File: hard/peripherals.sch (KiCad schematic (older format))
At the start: 16 parts, among them J3 PJ-3062-CO, U1 DNP, U2 ADXL345BCCZ-RL7

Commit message: attribute naming update
JLCPCB_Part_Number -> LCSC
DigiKey_Part_Number -> DigiKey
Mouser_Part_Number -> Mouser
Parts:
- D1026, D1027: JLCPCB_Part_Number C8056 -> (none); LCSC (none) -> C8056
- D1028: JLCPCB_Part_Number C32677 -> (none); LCSC (none) -> C32677
- D?: DigiKey (none) -> LTST-S270TBKT-5A-ND; DigiKey_Part_Number LTST-S270TBKT-5A-ND -> (none); JLCPCB_Part_Number C125115 -> (none); LCSC (none) -> C125115; Mouser (none) -> 859-LTST-S270TBKT; Mouser_Part_Number 859-LTST-S270TBKT -> (none)
- J3: JLCPCB_Part_Number C319113 -> (none); LCSC (none) -> C319113
- M?: JLCPCB_Part_Number C65189 -> (none); LCSC (none) -> C65189
- U1: DigiKey (none) -> ADXL362BCCZ-RL7CT-ND; DigiKey_Part_Number ADXL362BCCZ-RL7CT-ND -> (none); JLCPCB_Part_Number C59641 -> (none); LCSC (none) -> C59641
- U2: DigiKey (none) -> ADXL345BCCZ-RLCT-ND; DigiKey_Part_Number ADXL345BCCZ-RLCT-ND -> (none); JLCPCB_Part_Number C9667 -> (none); LCSC (none) -> C9667
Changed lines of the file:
@@
 F 2 "led_matrix:Sensors_AnalogDevices_ADXL345BCCZ-RL" H 8750 4300 50  0001 C CNN
 F 3 "https://www.analog.com/media/en/technical-documentation/data-sheets/ADXL345.pdf" H 8750 4800 50  0001 C CNN
-F 4 "ADXL345BCCZ-RLCT-ND" H 8750 4300 50  0001 C CNN "DigiKey_Part_Number"
-F 5 "C9667" H 8750 4300 50  0001 C CNN "JLCPCB_Part_Number"
+F 4 "ADXL345BCCZ-RLCT-ND" H 8750 4300 50  0001 C CNN "DigiKey"
+F 5 "C9667" H 8750 4300 50  0001 C CNN "LCSC"
 F 6 "Analog Devices Inc." H 8750 4300 50  0001 C CNN "MF"
 F 7 "ADXL345BCCZ-RL7" H 8750 4300 50  0001 C CNN "MPN"
@@
 F 2 "led_matrix:Connectors_XKB Connectivity_PJ-3062-CO" H 2400 2650 50  0001 C CNN
 F 3 "2002271743_XKB-Connectivity-PJ-3062-CO_C319113.pdf" H 2400 2650 50  0001 C CNN
-F 4 "" H 2400 2650 50  0001 C CNN "DigiKey_Part_Number"
-F 5 "" H 2400 2650 50  0001 C CNN "Mouser_Part_Number"
-F 6 "C319113" H 2400 2650 50  0001 C CNN "JLCPCB_Part_Number"
+F 4 "" H 2400 2650 50  0001 C CNN "DigiKey"
+F 5 "" H 2400 2650 50  0001 C CNN "Mouser"
+F 6 "C319113" H 2400 2650 50  0001 C CNN "LCSC"
 F 7 "XKB Connectivity" H 2400 2650 50  0001 C CNN "MF"
 F 8 "PJ-3062-CO" H 2400 2650 50  0001 C CNN "MPN"
@@
 F 2 "Package_TO_SOT_SMD:SOT-23" H 3250 3200 50  0001 C CNN
 F 3 "ProTek-Devices-PSM712-LF-T7_C32677.pdf" H 3250 3200 50  0001 C CNN
-F 4 "" H 3250 3200 50  0001 C CNN "DigiKey_Part_Number"
-F 5 "" H 3250 3200 50  0001 C CNN "Mouser_Part_Number"
-F 6 "C32677" H 3250 3200 50  0001 C CNN "JLCPCB_Part_Number"
+F 4 "" H 3250 3200 50  0001 C CNN "DigiKey"
+F 5 "" H 3250 3200 50  0001 C CNN "Mouser"
+F 6 "C32677" H 3250 3200 50  0001 C CNN "LCSC"
 F 7 "ProTek Devices" H 3250 3200 50  0001 C CNN "MF"
 F 8 "PSM712-LF-T7" H 3250 3200 50  0001 C CNN "MPN"
@@
 F 2 "Diode_SMD:D_MiniMELF" H 3750 3150 50  0001 C CNN
 F 3 "1812121407_Semtech-ZMM3V3_C8056.pdf" H 3750 3150 50  0001 C CNN
-F 4 "" V 3750 3150 50  0001 C CNN "DigiKey_Part_Number"
-F 5 "" V 3750 3150 50  0001 C CNN "Mouser_Part_Number"
-F 6 "C8056" V 3750 3150 50  0001 C CNN "JLCPCB_Part_Number"
+F 4 "" V 3750 3150 50  0001 C CNN "DigiKey"
+F 5 "" V 3750 3150 50  0001 C CNN "Mouser"
+F 6 "C8056" V 3750 3150 50  0001 C CNN "LCSC"
 F 7 "ZMM3V3" V 3750 3150 50  0001 C CNN "MF"
 F 8 "Semtech" V 3750 3150 50  0001 C CNN "MPN"
@@
 F 2 "Diode_SMD:D_MiniMELF" H 4250 3150 50  0001 C CNN
 F 3 "1812121407_Semtech-ZMM3V3_C8056.pdf" H 4250 3150 50  0001 C CNN
-F 4 "" V 4250 3150 50  0001 C CNN "DigiKey_Part_Number"
-F 5 "" V 4250 3150 50  0001 C CNN "Mouser_Part_Number"
-F 6 "C8056" V 4250 3150 50  0001 C CNN "JLCPCB_Part_Number"
+F 4 "" V 4250 3150 50  0001 C CNN "DigiKey"
+F 5 "" V 4250 3150 50  0001 C CNN "Mouser"
+F 6 "C8056" V 4250 3150 50  0001 C CNN "LCSC"
 F 7 "ZMM3V3" V 4250 3150 50  0001 C CNN "MF"
 F 8 "Semtech" V 4250 3150 50  0001 C CNN "MPN"
@@
 F 2 "led_matrix:Sensors_AnalogDevices_ADXL362BCCZ-RX" H 8600 2750 50  0001 C CNN
 F 3 "https://www.analog.com/media/en/technical-documentation/data-sheets/ADXL362.pdf" H 8600 3250 50  0001 C CNN
-F 4 "ADXL362BCCZ-RL7CT-ND" H 8500 2750 50  0001 C CNN "DigiKey_Part_Number"
-F 5 "C59641" H 8600 2750 50  0001 C CNN "JLCPCB_Part_Number"
+F 4 "ADXL362BCCZ-RL7CT-ND" H 8500 2750 50  0001 C CNN "DigiKey"
+F 5 "C59641" H 8600 2750 50  0001 C CNN "LCSC"
 F 6 "Analog Devices" H 8500 2750 50  0001 C CNN "MF"
 F 7 "ADXL362BCCZ-RL" H 8500 2750 50  0001 C CNN "MPN"
@@
 F 2 "led_matrix:LED_LiteOn_LTST-S270TBKT" H 3850 5400 50  0001 C CNN
 F 3 "https://datasheet.lcsc.com/szlcsc/1810231514_Lite-On-LTST-S270TBKT_C125115.pdf" H 3850 5400 50  0001 C CNN
-F 4 "LTST-S270TBKT-5A-ND" H 3800 5300 50  0001 C CNN "DigiKey_Part_Number"
-F 5 "859-LTST-S270TBKT" H 3800 5300 50  0001 C CNN "Mouser_Part_Number"
-F 6 "C125115" H 3800 5300 50  0001 C CNN "JLCPCB_Part_Number"
+F 4 "LTST-S270TBKT-5A-ND" H 3800 5300 50  0001 C CNN "DigiKey"
+F 5 "859-LTST-S270TBKT" H 3800 5300 50  0001 C CNN "Mouser"
+F 6 "C125115" H 3800 5300 50  0001 C CNN "LCSC"
 F 7 "Lite-On Inc." H 3800 5300 50  0001 C CNN "MF"
 F 8 "LTST-S270TBKT" H 3800 5300 50  0001 C CNN "MPN"
@@
 F 2 "Package_TO_SOT_SMD:SOT-23" H 4550 5950 50  0001 C CNN
 F 3 "https://assets.nexperia.com/documents/data-sheet/2N7002.pdf" H 3750 5950 50  0001 C CNN
-F 4 "C65189" H 4150 5850 50  0001 C CNN "JLCPCB_Part_Number"
+F 4 "C65189" H 4150 5850 50  0001 C CNN "LCSC"
 F 5 "Nexperia" H 4550 5950 50  0001 C CNN "MF"
 F 6 "2N7002,215" H 4550 5950 50  0001 C CNN "MPN"

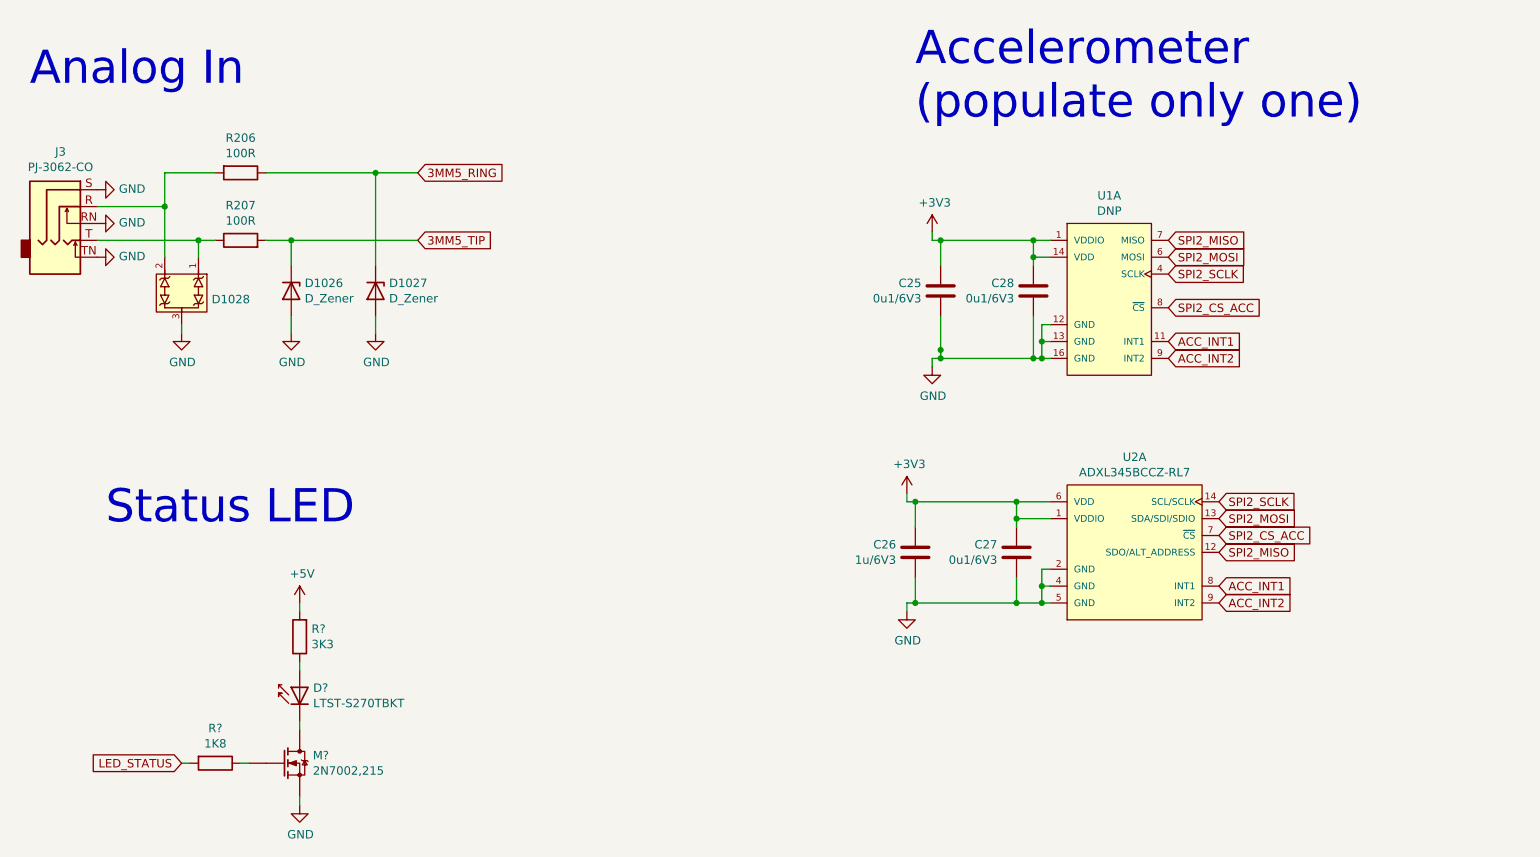
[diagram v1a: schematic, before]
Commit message: re-connect footprints
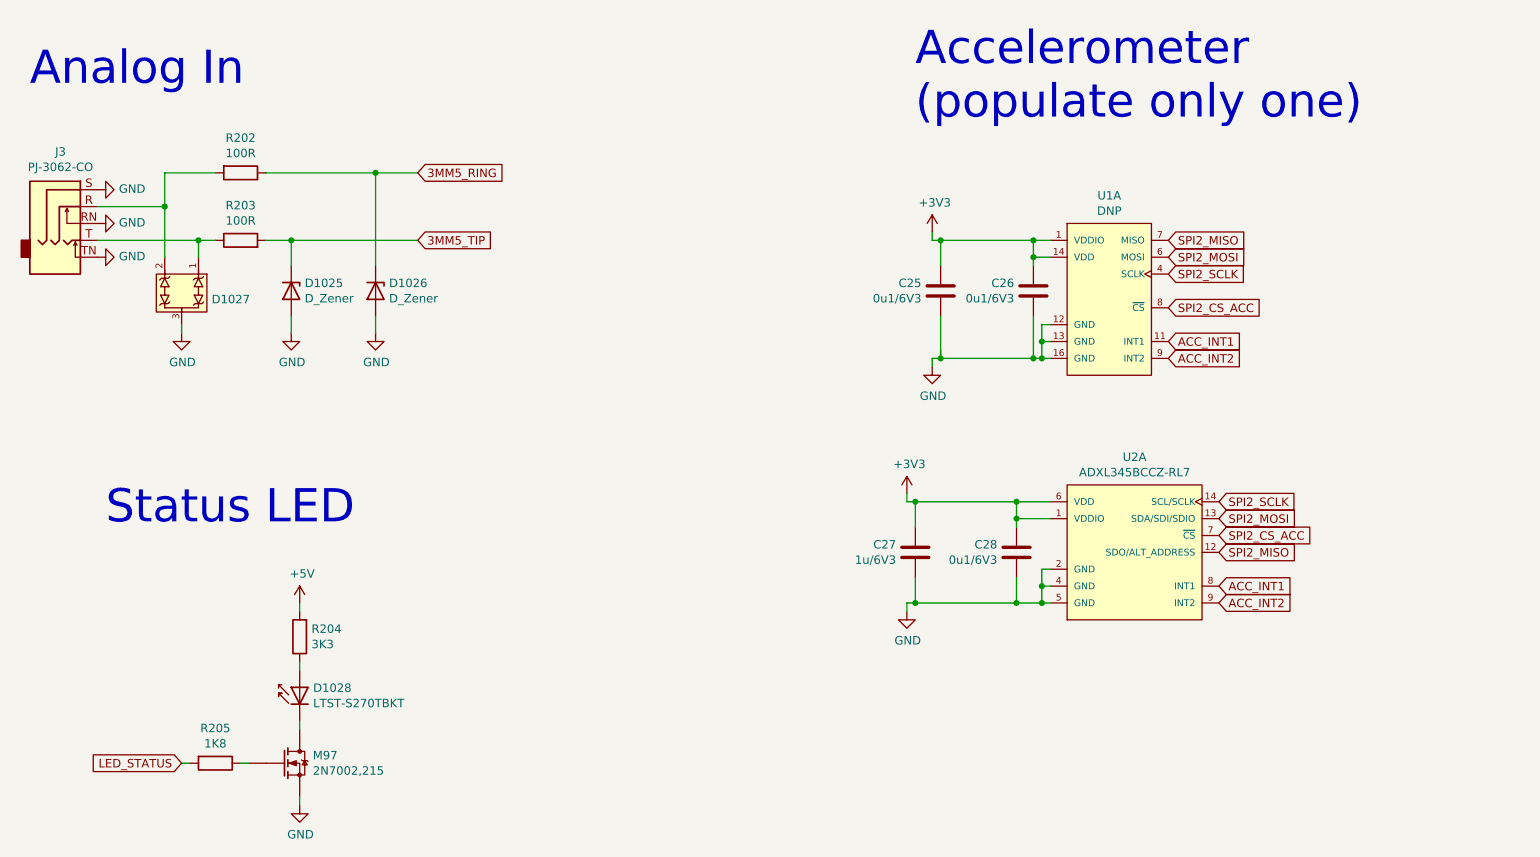
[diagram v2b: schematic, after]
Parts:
- gave numbers to parts that had none: 4
- renumbered C28 to C26, C26 to C27, C27 to C28, D1026 to D1025, D1027 to D1026, D1028 to D1027, R206 to R202, R207 to R203
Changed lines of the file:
@@
 $EndComp
 $Comp
-L Device:C C27
+L Device:C C28
 U 1 1 614359EF
 P 8050 4700
-F 0 "C27" H 7936 4654 50  0000 R CNN
+F 0 "C28" H 7936 4654 50  0000 R CNN
 F 1 "0u1/6V3" H 7936 4745 50  0000 R CNN
 F 2 "Capacitor_SMD:C_0402_1005Metric" H 8088 4550 50  0001 C CNN
@@
 $EndComp
 $Comp
-L Device:C C26
+L Device:C C27
 U 1 1 614361F4
 P 7450 4700
-F 0 "C26" H 7336 4654 50  0000 R CNN
+F 0 "C27" H 7336 4654 50  0000 R CNN
 F 1 "1u/6V3" H 7336 4745 50  0000 R CNN
 F 2 "Capacitor_SMD:C_0603_1608Metric" H 7488 4550 50  0001 C CNN
@@
 $EndComp
 $Comp
-L power:+3V3 #PWR0208
+L power:+3V3 #PWR0206
 U 1 1 61439963
 P 7400 4350
-F 0 "#PWR0208" H 7400 4200 50  0001 C CNN
+F 0 "#PWR0206" H 7400 4200 50  0001 C CNN
 F 1 "+3V3" H 7415 4523 50  0000 C CNN
 F 2 "" H 7400 4350 50  0001 C CNN
@@
 	8050 4500 8050 4550
 $Comp
-L power:GND #PWR0211
+L power:GND #PWR0208
 U 1 1 6143C822
 P 7400 5050
-F 0 "#PWR0211" H 7400 4800 50  0001 C CNN
+F 0 "#PWR0208" H 7400 4800 50  0001 C CNN
 F 1 "GND" H 7405 4877 50  0000 C CNN
 F 2 "" H 7400 5050 50  0001 C CNN
@@
 $EndComp
 $Comp
-L power:GND #PWR0202
+L power:GND #PWR0198
 U 1 1 6147785D
 P 2600 2550
-F 0 "#PWR0202" H 2600 2300 50  0001 C CNN
+F 0 "#PWR0198" H 2600 2300 50  0001 C CNN
 F 1 "GND" V 2605 2422 50  0000 R CNN
 F 2 "" H 2600 2550 50  0001 C CNN
@@
 $EndComp
 $Comp
-L power:GND #PWR0203
+L power:GND #PWR0199
 U 1 1 614784D6
 P 2600 2750
-F 0 "#PWR0203" H 2600 2500 50  0001 C CNN
+F 0 "#PWR0199" H 2600 2500 50  0001 C CNN
 F 1 "GND" V 2605 2622 50  0000 R CNN
 F 2 "" H 2600 2750 50  0001 C CNN
@@
 $EndComp
 $Comp
-L power:GND #PWR0204
+L power:GND #PWR0201
 U 1 1 614787FA
 P 2600 2950
-F 0 "#PWR0204" H 2600 2700 50  0001 C CNN
+F 0 "#PWR0201" H 2600 2700 50  0001 C CNN
 F 1 "GND" V 2605 2822 50  0000 R CNN
 F 2 "" H 2600 2950 50  0001 C CNN
@@
 3MM5_TIP
 $Comp
-L Device:R R206
+L Device:R R202
 U 1 1 6147E21F
 P 3450 2450
-F 0 "R206" V 3243 2450 50  0000 C CNN
+F 0 "R202" V 3243 2450 50  0000 C CNN
 F 1 "100R" V 3334 2450 50  0000 C CNN
 F 2 "Resistor_SMD:R_0603_1608Metric" V 3380 2450 50  0001 C CNN
@@
 $EndComp
 $Comp
-L Device:R R207
+L Device:R R203
 U 1 1 6147FCF6
 P 3450 2850
-F 0 "R207" V 3657 2850 50  0000 C CNN
+F 0 "R203" V 3657 2850 50  0000 C CNN
 F 1 "100R" V 3566 2850 50  0000 C CNN
 F 2 "Resistor_SMD:R_0603_1608Metric" V 3380 2850 50  0001 C CNN
@@
 $EndComp
 $Comp
-L led_matrix:PSM712-LF-T7 D1028
+L led_matrix:PSM712-LF-T7 D1027
 U 1 1 61497024
 P 3250 3200
-F 0 "D1028" V 3250 3228 50  0000 L CNN
+F 0 "D1027" V 3250 3228 50  0000 L CNN
 F 1 "PSM712-LF-T7" H 3250 3250 50  0001 C CNN
 F 2 "Package_TO_SOT_SMD:SOT-23" H 3250 3200 50  0001 C CNN
@@
 $EndComp
 $Comp
-L Device:D_Zener D1026
+L Device:D_Zener D1025
 U 1 1 614A4095
 P 3750 3150
-F 0 "D1026" V 3704 3230 50  0000 L CNN
+F 0 "D1025" V 3704 3230 50  0000 L CNN
 F 1 "D_Zener" V 3795 3230 50  0000 L CNN
 F 2 "Diode_SMD:D_MiniMELF" H 3750 3150 50  0001 C CNN
@@
 $EndComp
 $Comp
-L Device:D_Zener D1027
+L Device:D_Zener D1026
 U 1 1 614AA758
 P 4250 3150
-F 0 "D1027" V 4204 3230 50  0000 L CNN
+F 0 "D1026" V 4204 3230 50  0000 L CNN
 F 1 "D_Zener" V 4295 3230 50  0000 L CNN
 F 2 "Diode_SMD:D_MiniMELF" H 4250 3150 50  0001 C CNN
@@
 Connection ~ 4250 2450
 $Comp
-L power:GND #PWR0205
+L power:GND #PWR0202
 U 1 1 614B8C36
 P 3100 3400
-F 0 "#PWR0205" H 3100 3150 50  0001 C CNN
+F 0 "#PWR0202" H 3100 3150 50  0001 C CNN
 F 1 "GND" H 3105 3227 50  0000 C CNN
 F 2 "" H 3100 3400 50  0001 C CNN
@@
 $EndComp
 $Comp
-L power:GND #PWR0206
+L power:GND #PWR0203
 U 1 1 614B947F
 P 3750 3400
-F 0 "#PWR0206" H 3750 3150 50  0001 C CNN
+F 0 "#PWR0203" H 3750 3150 50  0001 C CNN
 F 1 "GND" H 3755 3227 50  0000 C CNN
 F 2 "" H 3750 3400 50  0001 C CNN
@@
 $EndComp
 $Comp
-L power:GND #PWR0207
+L power:GND #PWR0204
 U 1 1 614B9A2A
 P 4250 3400
-F 0 "#PWR0207" H 4250 3150 50  0001 C CNN
+F 0 "#PWR0204" H 4250 3150 50  0001 C CNN
 F 1 "GND" H 4255 3227 50  0000 C CNN
 F 2 "" H 4250 3400 50  0001 C CNN
@@
 SPI2_MISO
 $Comp
-L Device:C C28
+L Device:C C26
 U 1 1 6058FCE3
 P 8150 3150
-F 0 "C28" H 8036 3104 50  0000 R CNN
+F 0 "C26" H 8036 3104 50  0000 R CNN
 F 1 "0u1/6V3" H 8036 3195 50  0000 R CNN
 F 2 "Capacitor_SMD:C_0402_1005Metric" H 8188 3000 50  0001 C CNN
@@
 	7600 2850 7600 3000
 $Comp
-L power:+3V3 #PWR0201
+L power:+3V3 #PWR0200
 U 1 1 605930E4
 P 7550 2800
-F 0 "#PWR0201" H 7550 2650 50  0001 C CNN
+F 0 "#PWR0200" H 7550 2650 50  0001 C CNN
 F 1 "+3V3" H 7565 2973 50  0000 C CNN
 F 2 "" H 7550 2800 50  0001 C CNN
@@
 $EndComp
 $Comp
-L power:GND #PWR0209
+L power:GND #PWR0205
 U 1 1 60593C1E
 P 7550 3600
-F 0 "#PWR0209" H 7550 3350 50  0001 C CNN
+F 0 "#PWR0205" H 7550 3350 50  0001 C CNN
 F 1 "GND" H 7555 3427 50  0000 C CNN
 F 2 "" H 7550 3600 50  0001 C CNN
@@
 P 3800 5550
 AR Path="/6053C560/61753928" Ref="D?"  Part="1"
-AR Path="/6053C8CB/61753928" Ref="D?"  Part="1"
-F 0 "D?" V 3846 5470 50  0000 R CNN
+AR Path="/6053C8CB/61753928" Ref="D1028"  Part="1"
+F 0 "D1028" V 3846 5470 50  0000 R CNN
 F 1 "LTST-S270TBKT" V 3755 5470 50  0000 R CNN
 F 2 "led_matrix:LED_LiteOn_LTST-S270TBKT" H 3850 5400 50  0001 C CNN
@@
 P 3800 5200
 AR Path="/6053C560/6175392E" Ref="R?"  Part="1"
-AR Path="/6053C8CB/6175392E" Ref="R?"  Part="1"
-F 0 "R?" H 3730 5154 50  0000 R CNN
+AR Path="/6053C8CB/6175392E" Ref="R204"  Part="1"
+F 0 "R204" H 3730 5154 50  0000 R CNN
 F 1 "3K3" H 3730 5245 50  0000 R CNN
 F 2 "Resistor_SMD:R_0402_1005Metric" V 3730 5200 50  0001 C CNN
@@
 P 3750 5950
 AR Path="/6053C560/61753938" Ref="M?"  Part="1"
-AR Path="/6053C8CB/61753938" Ref="M?"  Part="1"
-F 0 "M?" H 3878 5996 50  0000 L CNN
+AR Path="/6053C8CB/61753938" Ref="M97"  Part="1"
+F 0 "M97" H 3878 5996 50  0000 L CNN
 F 1 "2N7002,215" H 3878 5905 50  0000 L CNN
 F 2 "Package_TO_SOT_SMD:SOT-23" H 4550 5950 50  0001 C CNN
@@
 P 3800 5000
 AR Path="/6053C560/6175393E" Ref="#PWR?"  Part="1"
-AR Path="/6053C8CB/6175393E" Ref="#PWR?"  Part="1"
-F 0 "#PWR?" H 3800 4850 50  0001 C CNN
+AR Path="/6053C8CB/6175393E" Ref="#PWR0207"  Part="1"
+F 0 "#PWR0207" H 3800 4850 50  0001 C CNN
 F 1 "+5V" H 3815 5173 50  0000 C CNN
 F 2 "" H 3800 5000 50  0001 C CNN
@@
 P 3300 5950
 AR Path="/6053C560/61753944" Ref="R?"  Part="1"
-AR Path="/6053C8CB/61753944" Ref="R?"  Part="1"
-F 0 "R?" V 3093 5950 50  0000 C CNN
+AR Path="/6053C8CB/61753944" Ref="R205"  Part="1"
+F 0 "R205" V 3093 5950 50  0000 C CNN
 F 1 "1K8" V 3184 5950 50  0000 C CNN
 F 2 "Resistor_SMD:R_0402_1005Metric" V 3230 5950 50  0001 C CNN
@@
 P 3800 6200
 AR Path="/6053C560/6175394D" Ref="#PWR?"  Part="1"
-AR Path="/6053C8CB/6175394D" Ref="#PWR?"  Part="1"
-F 0 "#PWR?" H 3800 5950 50  0001 C CNN
+AR Path="/6053C8CB/6175394D" Ref="#PWR0209"  Part="1"
+F 0 "#PWR0209" H 3800 5950 50  0001 C CNN
 F 1 "GND" H 3805 6027 50  0000 C CNN
 F 2 "" H 3800 6200 50  0001 C CNN
@@
 Text Notes 2650 4550 0    197  ~ 0
 Status LED
-Connection ~ 7600 3500
 Wire Wire Line
 	7600 3500 7600 3550

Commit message: updated footprints in preparation for connector 3d files
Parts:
- J3: footprint led_matrix:Connectors_XKB Connectivity_PJ-3062-CO -> led_matrix:Connectors_XKB-Connectivity_PJ-3062-CO
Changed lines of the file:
@@
 F 0 "J3" H 2382 2975 50  0000 C CNN
 F 1 "PJ-3062-CO" H 2382 2884 50  0000 C CNN
-F 2 "led_matrix:Connectors_XKB Connectivity_PJ-3062-CO" H 2400 2650 50  0001 C CNN
+F 2 "led_matrix:Connectors_XKB-Connectivity_PJ-3062-CO" H 2400 2650 50  0001 C CNN
 F 3 "2002271743_XKB-Connectivity-PJ-3062-CO_C319113.pdf" H 2400 2650 50  0001 C CNN
 F 4 "" H 2400 2650 50  0001 C CNN "DigiKey"
